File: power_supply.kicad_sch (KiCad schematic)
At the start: 41 parts, among them J3 BM02B-SRSS-TB, J4 5023820470, J5 USB_C_Receptacle_USB2.0, Q3 SQ3495EV-T1, SW3 D2F-L2-A1, SW4 D2F-L2-A, SW5 CAS-120TA, U16 AP2112K-3.3, U17 LTC4412xS6, U18 INA219BxD, U19 USBLC6-2SC6, U2 74LVC1G02, U7 TLV75515PDBVR, U8 AP7366-28W5-7

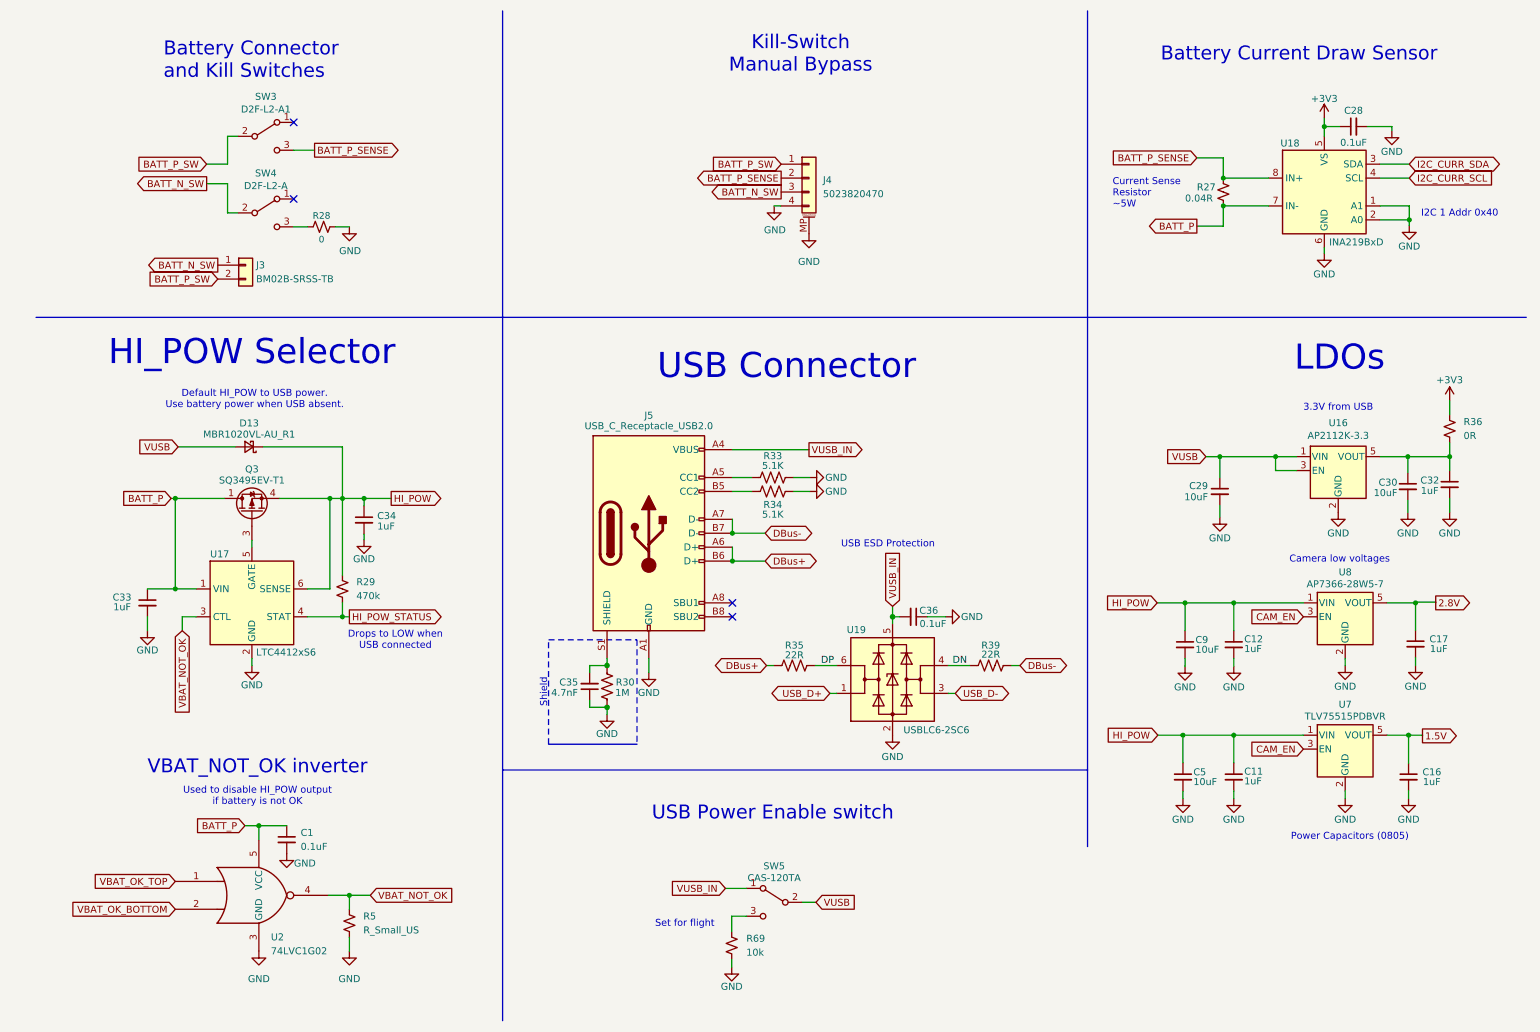
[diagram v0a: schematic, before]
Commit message: Fix ERC warnings
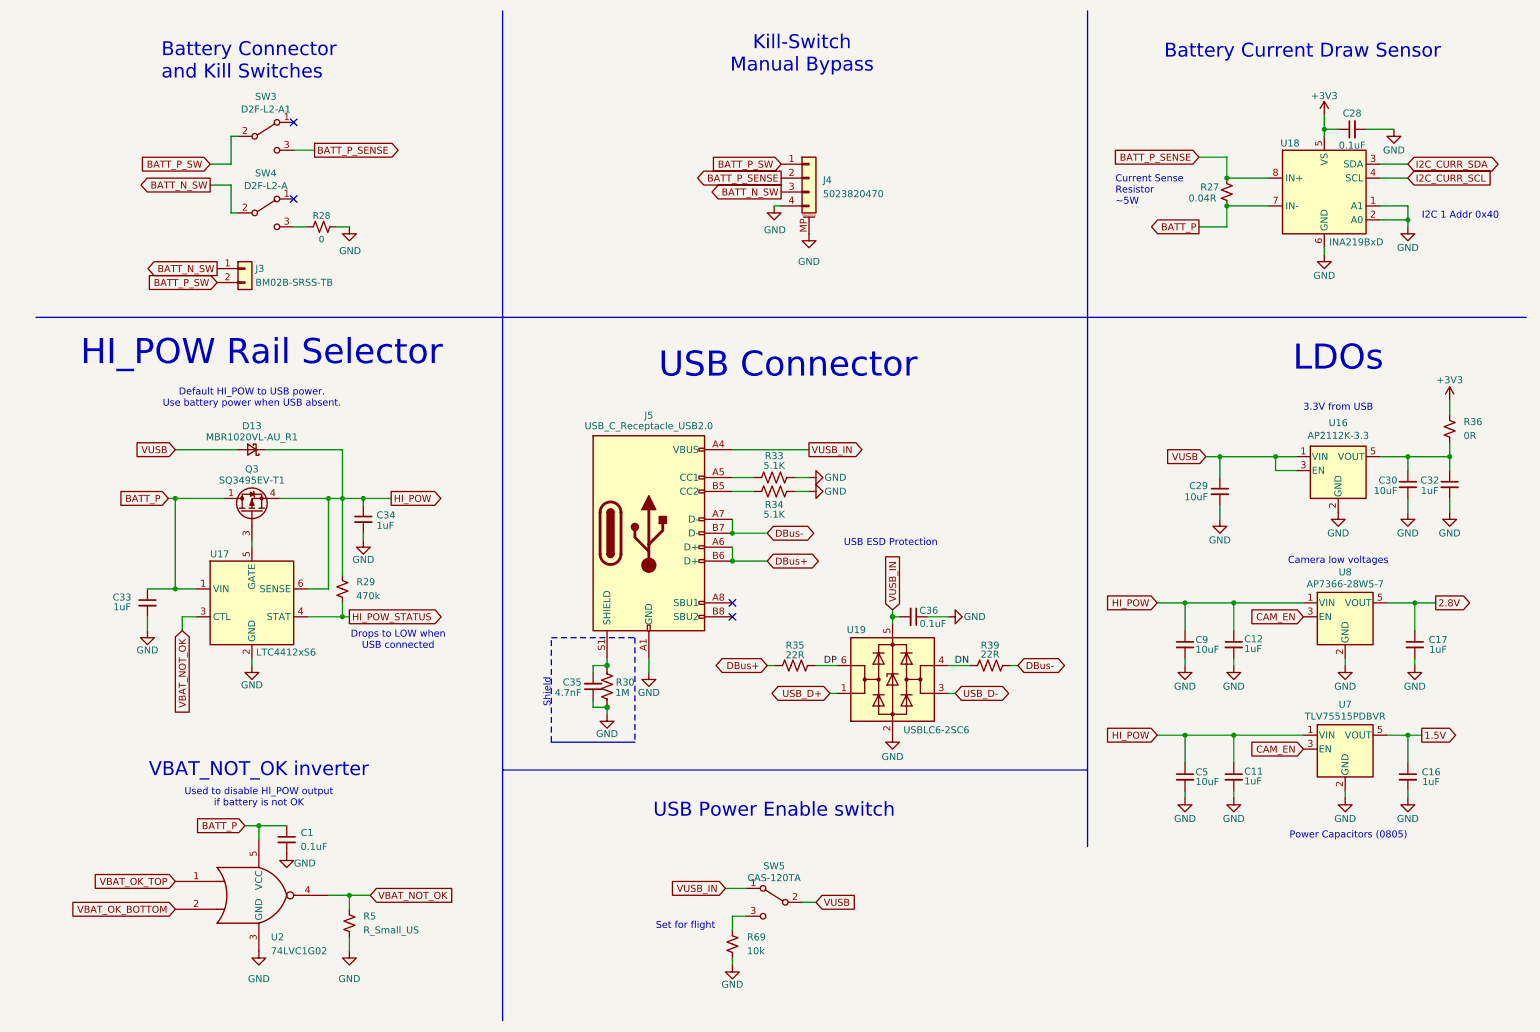
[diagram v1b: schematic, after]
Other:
- note added: "HI_POW Rail Selector"
- note removed: "HI_POW Selector"
- moved on the sheet: C28, C35, D13, J3, R27

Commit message: Reannotate schematic
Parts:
- renumbered C28 to C37, C30 to C38, C32 to C39, C29 to C40, C34 to C41, C33 to C42, C36 to C43, C9 to C44, C12 to C45, C17 to C46, C35 to C47, C5 to C48, C11 to C49, C16 to C50, C1 to C51, D13 to D6, J4 to J5, J3 to J6, J5 to J7, R27 to R32, R28 to R33, R36 to R34, R33 to R35, R34 to R36, R29 to R37, R35 to R38, R30 to R40, R5 to R41, R69 to R42, U18 to U14, U16 to U15, U17 to U16, U8 to U17, U19 to U18, U7 to U19, U2 to U20

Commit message: Fix inconsistencies in symbol fields
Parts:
- C51: footprint (none) -> Capacitor_SMD:C_0603_1608Metric
- R33: value 0 -> 0R
- R35, R36: value 5.1K -> 5.1k
- R37: footprint (none) -> Resistor_SMD:R_0603_1608Metric
- R41: value R_Small_US -> 470k; footprint (none) -> Resistor_SMD:R_0603_1608Metric
- U20: footprint (none) -> Package_TO_SOT_SMD:Texas_R-PDSO-G5_DCK-5
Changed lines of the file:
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@@
 			)
 		)
-		(property "Value" "0"
+		(property "Value" "0R"
 			(at 63.5 54.356 90)
 			(effects
@@
 			)
 		)
-		(property "Footprint" ""
+		(property "Footprint" "Resistor_SMD:R_0603_1608Metric"
 			(at 67.31 118.11 0)
 			(effects
@@
 			)
 		)
-		(property "Value" "R_Small_US"
+		(property "Value" "470k"
 			(at 71.12 180.3399 0)
 			(effects
@@
 			)
 		)
-		(property "Footprint" ""
+		(property "Footprint" "Resistor_SMD:R_0603_1608Metric"
 			(at 68.58 179.07 0)
 			(effects
@@
 			)
 		)
-		(property "Footprint" ""
+		(property "Footprint" "Capacitor_SMD:C_0603_1608Metric"
 			(at 57.15 163.83 0)
 			(effects
@@
 			)
 		)
-		(property "Value" "5.1K"
+		(property "Value" "5.1k"
 			(at 146.05 104.521 90)
 			(effects
@@
 			)
 		)
-		(property "Value" "5.1K"
+		(property "Value" "5.1k"
 			(at 146.05 95.631 90)
 			(effects
@@
 			)
 		)
-		(property "Footprint" ""
+		(property "Footprint" "Package_TO_SOT_SMD:Texas_R-PDSO-G5_DCK-5"
 			(at 52.07 173.99 0)
 			(effects

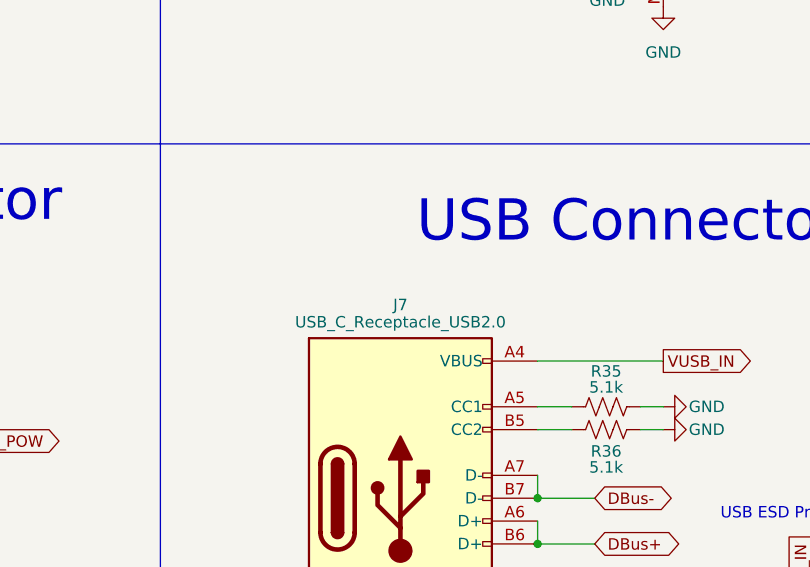
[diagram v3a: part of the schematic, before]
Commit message: Add MPNs
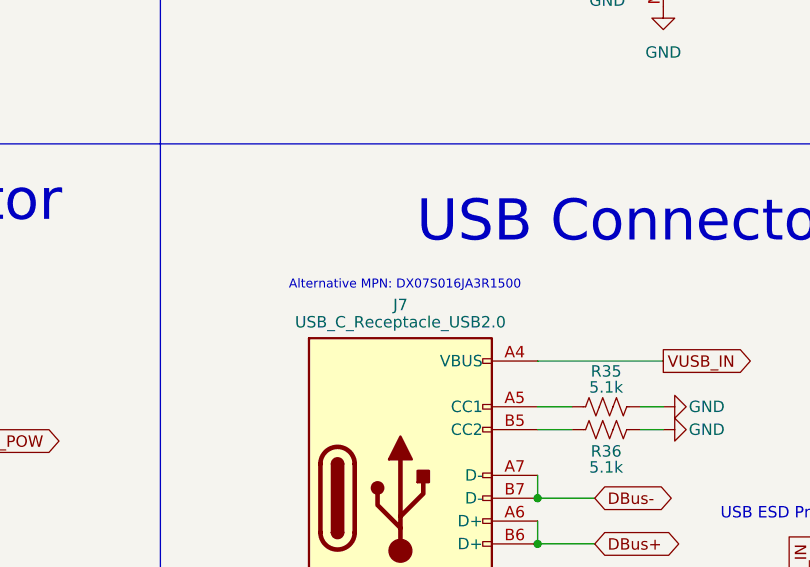
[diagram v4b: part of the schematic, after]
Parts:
- C37, C43, C51: Manufacturer_Part_Number (none) -> GCM188L81H104KA57D
- C38, C40: Manufacturer_Part_Number (none) -> CGA4J1X7S1C106K125AE
- C39: Manufacturer_Part_Number (none) -> CGA4J1X8L1H105K125AE
- C41, C42, C45, C46, C49, C50: Manufacturer_Part_Number (none) -> GCM188R71E105KA64D
- C44, C48: Manufacturer_Part_Number (none) -> GRT188R61C106ME13D
- C47: Manufacturer_Part_Number (none) -> GRM1885C1H472JA01D
- D6: Manufacturer_Part_Number (none) -> MBR1020VL-AU_R1_000A1
- J6: Manufacturer_Part_Number (none) -> BM02B-SRSS-TB
- J7: Manufacturer_Part_Number (none) -> TYPE-C-31-M-12
- Q3: Manufacturer_Part_Number (none) -> SQ3495EV-T1_GE3
- R32: Manufacturer_Part_Number (none) -> CRA2512-FZ-R040ELF
- R33: Manufacturer_Part_Number (none) -> ERJ-3GEY0R00V
- R34: Manufacturer_Part_Number (none) -> ERJ-1TY0R00U
- R35, R36: Manufacturer_Part_Number (none) -> ERJ-3GEYJ512V
- R37, R41: Manufacturer_Part_Number (none) -> ERJ-3GEYJ474V
- R38, R39: Manufacturer_Part_Number (none) -> ERJ-3EKF22R0V
- R40: Manufacturer_Part_Number (none) -> ERJ-3EKF1004V
- R42: Manufacturer_Part_Number (none) -> ERJ-3EKF1002V
- SW3: Manufacturer_Part_Number (none) -> D2F-L2-A1
- SW4: Manufacturer_Part_Number (none) -> D2F-L2-A
- SW5: Manufacturer_Part_Number (none) -> CAS-120TA
- U14: Manufacturer_Part_Number (none) -> INA219BIDR
- U15: Manufacturer_Part_Number (none) -> AP2112K-3.3TRG1
- U16: Manufacturer_Part_Number (none) -> LTC4412IS6#TRMPBF
- U17: Manufacturer_Part_Number (none) -> AP7366-28W5-7
- U18: Manufacturer_Part_Number (none) -> USBLC6-2SC6
- U19: Manufacturer_Part_Number (none) -> TLV75515PDBVR
- U20: Manufacturer_Part_Number (none) -> SN74LVC1G02DCKR
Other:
- note added: "Alternative MPN: DX07S016JA3R1500"

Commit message: Add battery connectors
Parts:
- removed J5: 5023820470, Connector_Molex:Molex_CLIK-Mate_502382-0470_1x04-1MP_P1.25mm_Vertical, symbol Connector_Generic_MountingPin:Conn_01x04_MountingPin
- removed SW4: D2F-L2-A, solarpanels:D2F-L2-A, symbol Switch:SW_SPDT
- added J5, J8, J9: BM02B-SRSS-TB, Connector_JST:JST_SH_BM02B-SRSS-TB_1x02-1MP_P1.00mm_Vertical, symbol Connector_Generic:Conn_01x02
- added R43: 470k, Resistor_SMD:R_0603_1608Metric, symbol Device:R_Small_US
- added R44, R45, R46, R47: 0R, Resistor_SMD:R_0603_1608Metric, symbol Device:R_Small_US
- SW3: value D2F-L2-A1 -> CAS-120TA; footprint solarpanels:D2F-L2-A1 -> cameraboard:CAS-120TA; Manufacturer_Part_Number D2F-L2-A1 -> CAS-120TA
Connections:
- net BATT_N_SW: now also R33.1, J5.1 (Pin_1), J8.1 (Pin_1), J9.1 (Pin_1)
- net BATT_P: now also R43.1
- net BATT_P_SENSE: now also SW3.2 (B); no longer SW3.3 (C)
- net BATT_P_SW: now also SW3.1 (A), R44.1, R45.1, R46.1, R47.1; no longer J6.2 (Pin_2), SW3.2 (B)
- net VBAT_OK_TOP: no longer names the net of U20.1
- net VBAT_OK_TOP: now also R43.2
- new net: J6.2 (Pin_2), R45.2
- new net: J8.2 (Pin_2), R46.2
- new net: J9.2 (Pin_2), R47.2
- new net: J5.2 (Pin_2), R44.2
- no-connect marks 4 -> 3
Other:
- note added: "Battery Connectors"
- note added: "Battery Enable Switch"
- note removed: "Battery Connector and Kill Switches"
- note removed: "Kill-Switch Manual Bypass"
